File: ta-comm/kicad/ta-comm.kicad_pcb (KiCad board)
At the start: 4 copper layers, 45 x 45 mm, 55 parts, among them IC1 CC1110F32RHHR, IC2 F2972NEGK, IC3 RFFM6404, IC4 STA0693A, J1 Conn_01x16, J2 Conn_01x16, J3 A-1JB, J4 Conn_01x04, J5 Conn_01x04, Y1 FOX924B-27

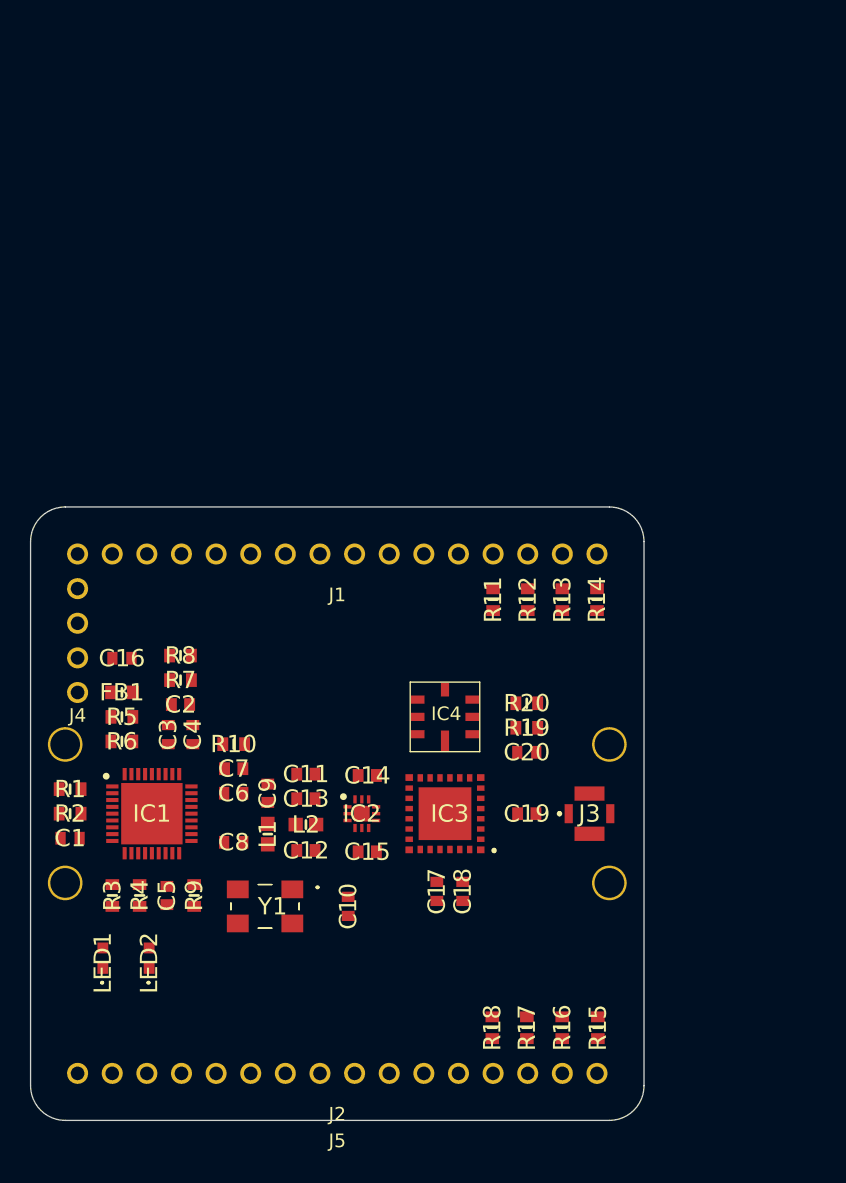
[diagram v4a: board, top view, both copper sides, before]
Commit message: Updates communication board schematic and PCB
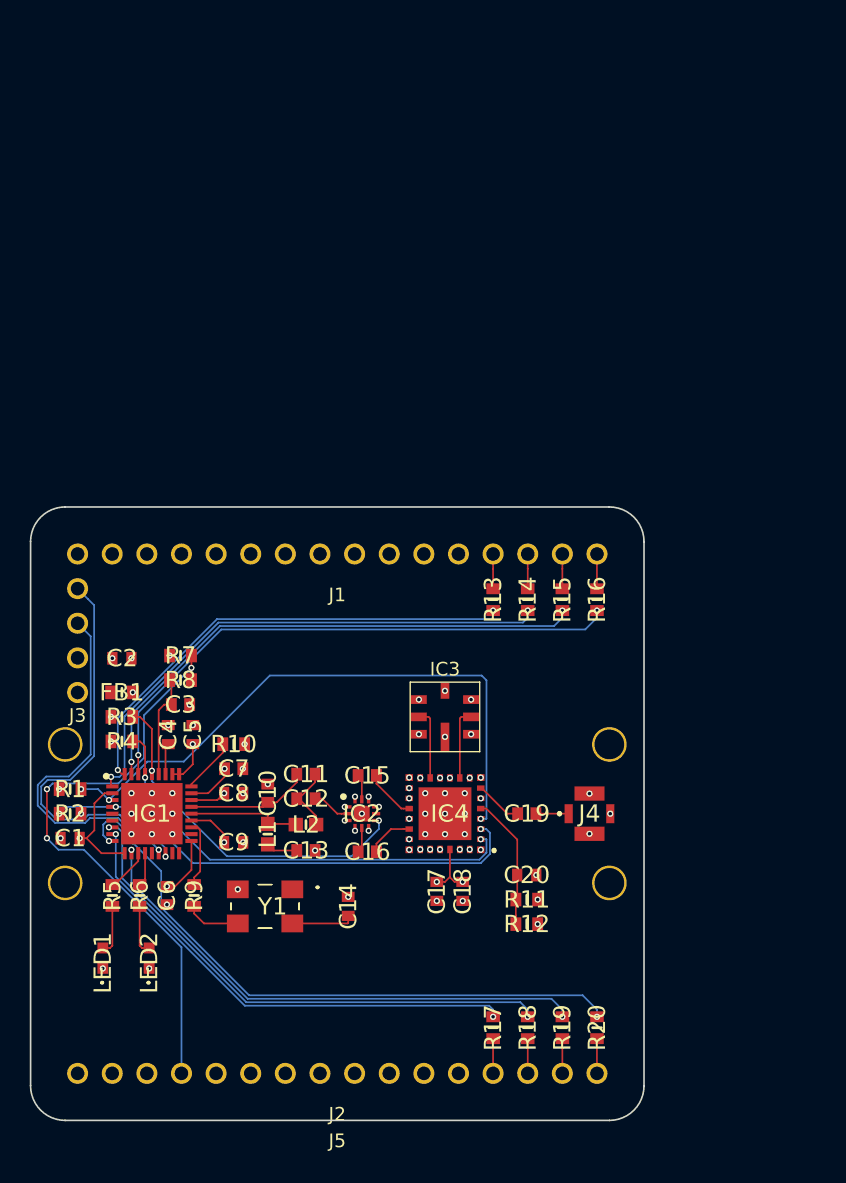
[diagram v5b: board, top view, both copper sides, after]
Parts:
- C10: value 0603ZC104KAT2A -> VJ0603A3R9BXQCW1BC; footprint ta-comm:CAPC1608X90N -> ta-comm:CAPC1608X87N
- C14, C5: value 885012006010 -> 0603ZC104KAT2A; footprint ta-comm:CAPC1608X87N -> ta-comm:CAPC1608X90N
- C16: value GRM188R71A225KE15D -> 885012006010; footprint ta-comm:CAPC1608X90N -> ta-comm:CAPC1608X87N
- C2: value 885012006014 -> GRM188R71A225KE15D; footprint ta-comm:CAPC1608X87N -> ta-comm:CAPC1608X90N
- C3: value 0603ZC105KAT2A -> 885012006014; footprint ta-comm:CAPC1608X90N -> ta-comm:CAPC1608X87N
- C4: value 0603ZC104KAT2A -> 0603ZC105KAT2A
- C6: value 0603ZC104KAT2A -> 885012006010; footprint ta-comm:CAPC1608X90N -> ta-comm:CAPC1608X87N
- C9: value VJ0603A3R9BXQCW1BC -> 0603ZC104KAT2A; footprint ta-comm:CAPC1608X87N -> ta-comm:CAPC1608X90N
- IC2: footprint QFN50P200X200X55-13N-D -> ta-comm:QFN50P200X200X55-13N-D
- IC3: value RFFM6404 -> STA0693A; footprint ta-comm:RFFM6404 -> ta-comm:STA0693A
- IC4: value STA0693A -> RFFM6404; footprint ta-comm:STA0693A -> ta-comm:RFFM6404
- J3: value A-1JB -> Conn_01x04; footprint ta-comm:A1JB -> ta-comm:PinSocket_1x4_TartanArtibeus
- J4: value Conn_01x04 -> A-1JB; footprint ta-comm:PinSocket_1x4_TartanArtibeus -> ta-comm:A1JB
- R11: value MCT06030C1000FP500 -> MCT06030C6801FP500
- R12: value MCT06030C1000FP500 -> MCT06030C1501FP500
- R19: value MCT06030C6801FP500 -> MCT06030C1000FP500
- R20: value MCT06030C1501FP500 -> MCT06030C1000FP500
- R7: value MCT06030C1001FP500 -> MCT06030C3302FP500
- R8: value MCT06030C3302FP500 -> MCT06030C1001FP500
- moved J3 39.6 mm to (135.9, 95.3), turned to 0 degrees
- moved J4 39.6 mm to (173.5, 108.0), turned to 180 degrees
- moved R15 31.5 mm to (171.5, 92.3), turned to 90 degrees
- moved R16 31.5 mm to (174.1, 92.3), turned to 90 degrees
- moved R20 24.4 mm to (174.1, 123.7), turned to 270 degrees
- moved R12 23.8 mm to (168.9, 116.1), turned to 180 degrees
- moved C16 22.9 mm to (157.2, 110.8), turned to 0 degrees
- moved R19 22.2 mm to (171.5, 123.7), turned to 270 degrees
- moved R11 22.1 mm to (168.9, 114.3), turned to 0 degrees
- moved R3 13.1 mm to (139.2, 100.9), turned to 180 degrees
- moved R5 13.1 mm to (138.5, 114.0), turned to 270 degrees
- moved C5 12.0 mm to (144.4, 102.2), turned to 90 degrees
- moved R4 11.4 mm to (139.2, 102.7), turned to 180 degrees
- moved R6 11.4 mm to (140.5, 114.0), turned to 270 degrees
- moved C10 10.2 mm to (149.9, 106.5)
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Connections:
- C11 pad 1: Net-(C11-Pad1) -> Net-(C10-Pad1)
- C12 pad 1: Net-(C12-Pad1) -> Net-(C11-Pad2)
- C12 pad 2: GND -> Net-(C12-Pad2)
- C13 pad 1: Net-(C11-Pad2) -> Net-(C13-Pad1)
- C13 pad 2: Net-(C13-Pad2) -> GND
- C14 pad 2: Net-(C14-Pad2) -> GND
- C16 pad 1: /VDD_FILT -> Net-(C16-Pad1)
- C16 pad 2: GND -> Net-(C16-Pad2)
- C2 pad 1: Net-(C2-Pad1) -> /VDD_FILT
- C5 pad 1: Net-(C5-Pad1) -> /VDD_FILT
- C6 pad 1: Net-(C6-Pad1) -> /VDD_FILT
- C7 pad 1: Net-(C7-Pad1) -> /VDD_FILT
- C9 pad 1: Net-(C11-Pad1) -> /VDD_FILT
- IC1 pad 19: Net-(C5-Pad1) -> /VDD_FILT
- IC1 pad 24: Net-(C11-Pad1) -> Net-(C10-Pad1)
- IC1 pad 25: Net-(C6-Pad1) -> /VDD_FILT
- IC1 pad 26: Net-(C7-Pad1) -> /VDD_FILT
- IC1 pad 28: Net-(C4-Pad1) -> /VDD_FILT
- IC1 pad 29: Net-(C4-Pad1) -> /VDD_FILT
- IC1 pad 30: Net-(C3-Pad1) -> Net-(C4-Pad1)
- IC1 pad 31: Net-(C2-Pad1) -> Net-(C3-Pad1)
- IC2 pad 11: Net-(C14-Pad1) -> Net-(C15-Pad1)
- IC2 pad 2: Net-(C13-Pad2) -> Net-(C12-Pad2)
- IC2 pad 5: Net-(C15-Pad1) -> Net-(C16-Pad1)
- IC3 pad 2: /TX_MODE -> Net-(IC3-Pad2)
- IC3 pad 3: /RF_EN -> GND
- IC3 pad 4: /RF_BYP -> GND
- IC3 pad 5: Net-(C20-Pad1) -> GND
- IC3 pad 6: GND -> Net-(IC3-Pad6)
- IC3 pad 7: Net-(C19-Pad1) -> GND
- IC4 pad 2: Net-(IC3-Pad10) -> /TX_MODE
- IC4 pad 3: GND -> /RF_EN
- IC4 pad 4: GND -> /RF_BYP
- IC4 pad 5: GND -> Net-(C20-Pad1)
- IC4 pad 6: Net-(IC3-Pad13) -> GND
- IC4 pad 7: GND -> Net-(C19-Pad1)
- J3 pad 1: Net-(C19-Pad2) -> VDD
- J3 pad 3: GND -> /PDIO
- J3 pad 4: GND -> /PCLK
- J4 pad 1: VDD -> Net-(C19-Pad2)
- J4 pad 3: /PDIO -> GND
- J4 pad 4: /PCLK -> GND
- L1 pad 2: Net-(C12-Pad1) -> Net-(C13-Pad1)
- R11 pad 1: /RTS0 -> Net-(C20-Pad1)
- R11 pad 2: Net-(J1-Pad13) -> GND
- R12 pad 1: /CTS0 -> /VDD_FILT
- R12 pad 2: Net-(J1-Pad14) -> Net-(C20-Pad1)
- R13 pad 1: /RX0 -> /RTS0
- R13 pad 2: Net-(J1-Pad15) -> Net-(J1-Pad13)
- R14 pad 1: /TX0 -> /CTS0
- R14 pad 2: Net-(J1-Pad16) -> Net-(J1-Pad14)
- R15 pad 1: /TX1 -> /RX0
- R15 pad 2: Net-(J2-Pad16) -> Net-(J1-Pad15)
- R16 pad 1: /RX1 -> /TX0
- R16 pad 2: Net-(J2-Pad15) -> Net-(J1-Pad16)
- R17 pad 1: /CTS1 -> /RTS1
- R17 pad 2: Net-(J2-Pad14) -> Net-(J2-Pad13)
- R18 pad 1: /RTS1 -> /CTS1
- R18 pad 2: Net-(J2-Pad13) -> Net-(J2-Pad14)
- R19 pad 1: Net-(C20-Pad1) -> /RX1
- R19 pad 2: GND -> Net-(J2-Pad15)
- R2 pad 1: /RF_EN -> /VDD_FILT
- R2 pad 2: /VDD_FILT -> /RF_EN
- R20 pad 1: /VDD_FILT -> /TX1
- R20 pad 2: Net-(C20-Pad1) -> Net-(J2-Pad16)
- R3 pad 1: /LED1 -> /RX_MODE
- R3 pad 2: Net-(LED1-Pad2) -> GND
- R4 pad 1: /LED2 -> /TX_MODE
- R4 pad 2: Net-(LED2-Pad2) -> GND
- R5 pad 1: /RX_MODE -> /LED1
- R5 pad 2: GND -> Net-(LED1-Pad2)
- R6 pad 1: /TX_MODE -> /LED2
- R6 pad 2: GND -> Net-(LED2-Pad2)
- R7 pad 1: Net-(C2-Pad1) -> /VDD_FILT
- R8 pad 2: /VDD_FILT -> Net-(C3-Pad1)
- Y1 pad 4: Net-(C10-Pad1) -> Net-(C14-Pad1)
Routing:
- net /TX1: track 0.00 -> 45.8 mm, vias 0 -> 2
- net /RF_BYP: track 0.00 -> 44.6 mm, vias 0 -> 3
- net /D0: track 0.00 -> 43.9 mm, vias 0 -> 3
- net /TX0: track 0.00 -> 41.6 mm, vias 0 -> 2
- net /RX0: track 0.00 -> 39.5 mm, vias 0 -> 2
- net /CTS0: track 0.00 -> 39.1 mm, vias 0 -> 2
- net /CTS1: track 0.00 -> 38.8 mm, vias 0 -> 2
- net /RX1: track 0.00 -> 38.4 mm, vias 0 -> 2
- net /RF_EN: track 0.00 -> 36.1 mm, vias 0 -> 3
- net /RTS0: track 0.00 -> 35.5 mm, vias 0 -> 2
- net /RTS1: track 0.00 -> 35.4 mm, vias 0 -> 2
- net /TX_MODE: track 0.00 -> 33.0 mm, vias 0 -> 2
- net /PCLK: track 0.00 -> 30.3 mm, vias 0 -> 1
- net /VDD_FILT: track 0.00 -> 29.7 mm, vias 0 -> 15
- net /PDIO: track 0.00 -> 26.9 mm, vias 0 -> 1
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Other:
- rule pad_to_mask_clearance: 0.0508 -> 0.051

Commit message: Completes communication board PCB
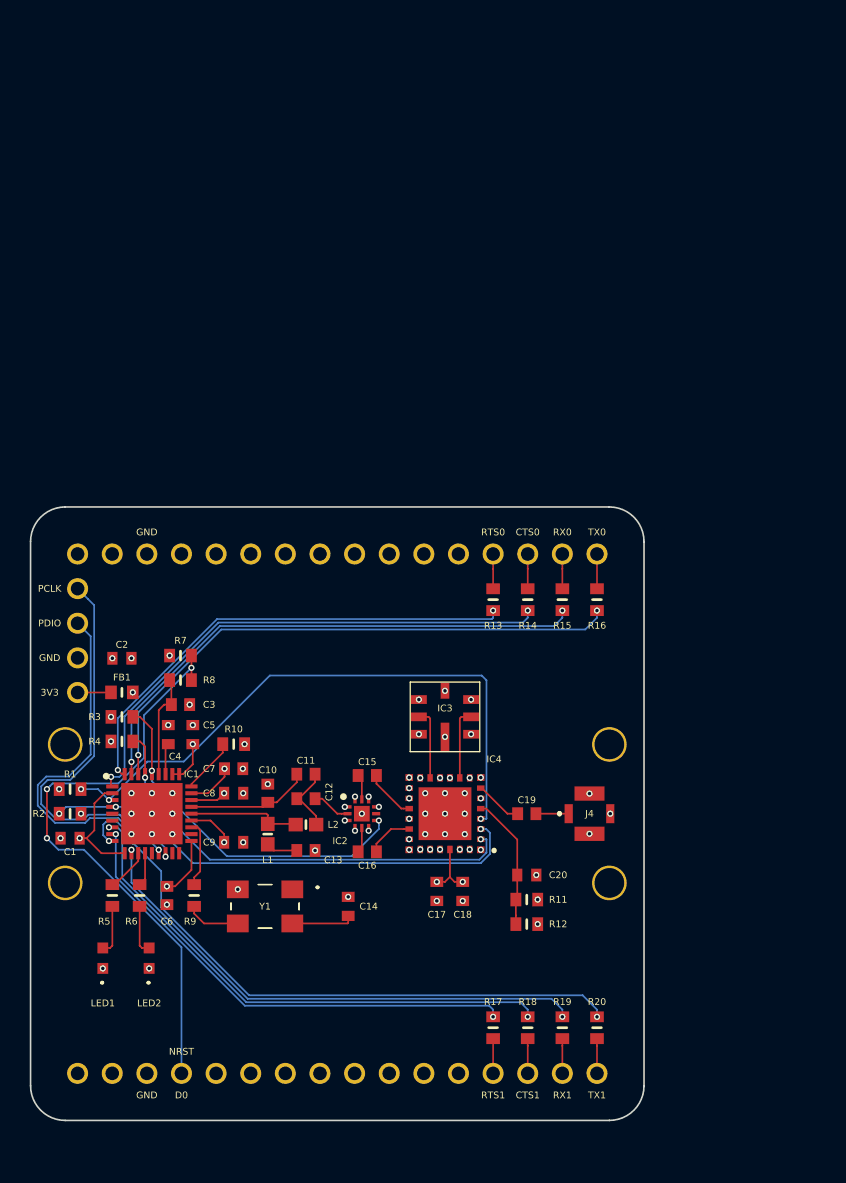
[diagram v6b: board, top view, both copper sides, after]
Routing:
- net VDD: track 0.00 -> 2.45 mm
- added copper zone on In2.Cu, net /VDD_FILT
- added copper zone on In1.Cu, net GND
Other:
- board text added: "3V3"
- board text added: "C1"
- board text added: "C10"
- board text added: "C11"
- board text added: "C12"
- board text added: "C13"
- board text added: "C14"
- board text added: "C15"
- board text added: "C16"
- board text added: "C17"
- board text added: "C18"
- board text added: "C19"
- board text added: "C2"
- board text added: "C20"
- board text added: "C3"
- board text added: "C4"
- board text added: "C5"
- board text added: "C6"
- board text added: "C7"
- board text added: "C8"
- board text added: "C9"
- board text added: "CTS0"
- board text added: "CTS1"
- board text added: "D0"
- board text added: "FB1"
- board text added: "GND"
- board text added: "IC1"
- board text added: "IC2"
- board text added: "IC3"
- board text added: "IC4"
- board text added: "J4"
- board text added: "L1"
- board text added: "L2"
- board text added: "LED1"
- board text added: "LED2"
- board text added: "NRST"
- board text added: "PCLK"
- board text added: "PDIO"
- board text added: "R1"
- board text added: "R10"
- board text added: "R11"
- board text added: "R12"
- board text added: "R13"
- board text added: "R14"
- board text added: "R15"
- board text added: "R16"
- board text added: "R17"
- board text added: "R18"
- board text added: "R19"
- board text added: "R2"
- board text added: "R20"
- board text added: "R3"
- board text added: "R4"
- board text added: "R5"
- board text added: "R6"
- board text added: "R7"
- board text added: "R8"
- board text added: "R9"
- board text added: "RTS0"
- board text added: "RTS1"
- board text added: "RX0"
- board text added: "RX1"
- board text added: "TX0"
- board text added: "TX1"
- board text added: "Y1"

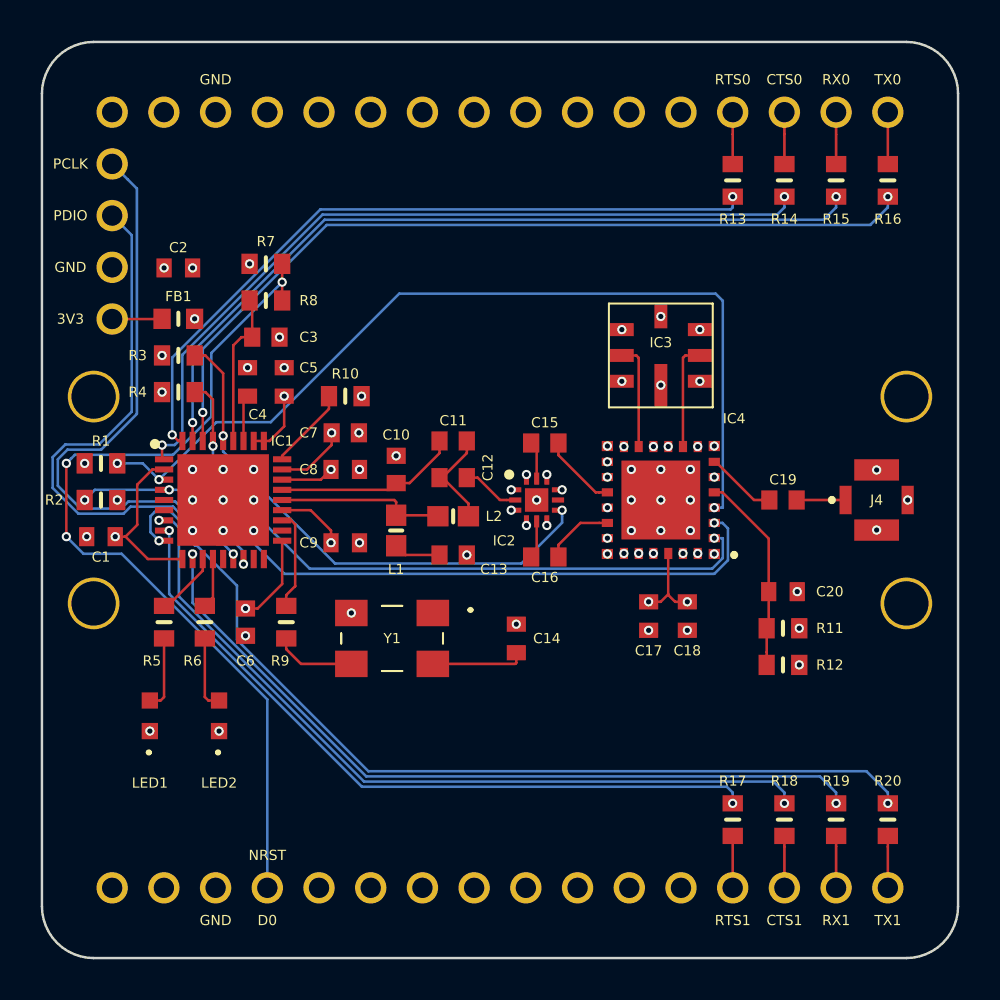
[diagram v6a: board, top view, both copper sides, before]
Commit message: Updates communication board PCB to move vias outside of pads
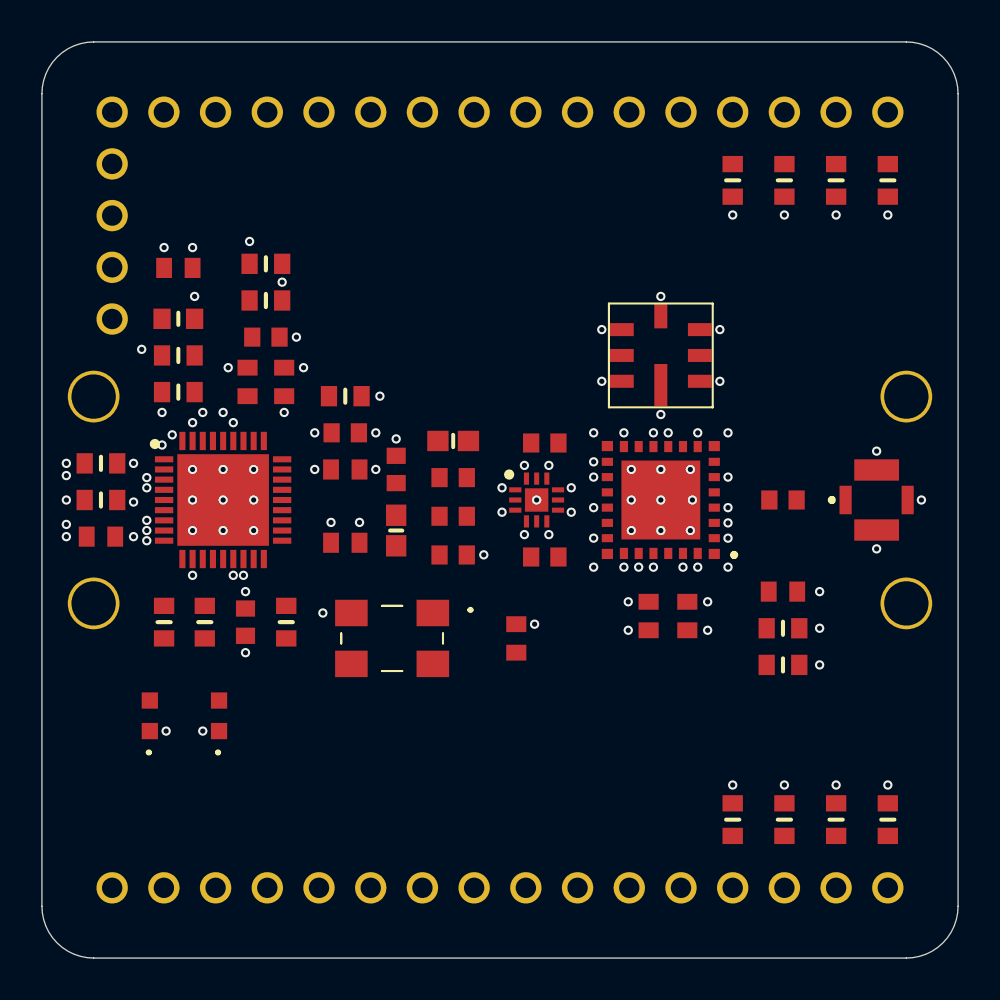
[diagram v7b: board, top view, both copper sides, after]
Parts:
- moved C11 3.70 mm to (152.7, 108.8)
- moved L2 3.70 mm to (152.7, 105.1)
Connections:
- C11 pad 1: Net-(C10-Pad1) -> Net-(C11-Pad1)
- IC1 pad 23: Net-(IC1-Pad23) -> Net-(C11-Pad1)
- L1 pad 1: Net-(IC1-Pad23) -> Net-(C11-Pad1)
- L2 pad 1: Net-(IC1-Pad23) -> Net-(C10-Pad1)
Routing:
- net /TX1: track 45.8 -> 0.00 mm
- net /RF_BYP: track 44.6 -> 0.00 mm
- net /D0: track 43.9 -> 0.00 mm
- net /TX0: track 41.6 -> 0.00 mm
- net /RX0: track 39.5 -> 0.00 mm
- net /CTS0: track 39.1 -> 0.00 mm
- net /CTS1: track 38.8 -> 0.00 mm
- net /RX1: track 38.4 -> 0.00 mm
- net /RF_EN: track 36.1 -> 0.00 mm
- net /RTS0: track 35.5 -> 0.00 mm
- net /RTS1: track 35.4 -> 0.00 mm
- net /TX_MODE: track 33.0 -> 0.00 mm
- net /PCLK: track 30.3 -> 0.00 mm
- net /VDD_FILT: track 29.7 -> 0.00 mm
- net /PDIO: track 26.9 -> 0.00 mm
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- removed copper zone on In2.Cu, net /VDD_FILT
- removed copper zone on In1.Cu, net GND
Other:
- rule pad_to_mask_clearance: 0.051 -> 0.0508
- board text removed: "3V3"
- board text removed: "C1"
- board text removed: "C10"
- board text removed: "C11"
- board text removed: "C12"
- board text removed: "C13"
- board text removed: "C14"
- board text removed: "C15"
- board text removed: "C16"
- board text removed: "C17"
- board text removed: "C18"
- board text removed: "C19"
- board text removed: "C2"
- board text removed: "C20"
- board text removed: "C3"
- board text removed: "C4"
- board text removed: "C5"
- board text removed: "C6"
- board text removed: "C7"
- board text removed: "C8"
- board text removed: "C9"
- board text removed: "CTS0"
- board text removed: "CTS1"
- board text removed: "D0"
- board text removed: "FB1"
- board text removed: "GND"
- board text removed: "IC1"
- board text removed: "IC2"
- board text removed: "IC3"
- board text removed: "IC4"
- board text removed: "J4"
- board text removed: "L1"
- board text removed: "L2"
- board text removed: "LED1"
- board text removed: "LED2"
- board text removed: "NRST"
- board text removed: "PCLK"
- board text removed: "PDIO"
- board text removed: "R1"
- board text removed: "R10"
- board text removed: "R11"
- board text removed: "R12"
- board text removed: "R13"
- board text removed: "R14"
- board text removed: "R15"
- board text removed: "R16"
- board text removed: "R17"
- board text removed: "R18"
- board text removed: "R19"
- board text removed: "R2"
- board text removed: "R20"
- board text removed: "R3"
- board text removed: "R4"
- board text removed: "R5"
- board text removed: "R6"
- board text removed: "R7"
- board text removed: "R8"
- board text removed: "R9"
- board text removed: "RTS0"
- board text removed: "RTS1"
- board text removed: "RX0"
- board text removed: "RX1"
- board text removed: "TX0"
- board text removed: "TX1"
- board text removed: "Y1"
